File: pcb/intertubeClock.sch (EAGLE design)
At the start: 174 parts, among them Q1 TP5322K1-G, Q10 TP5322K1-G, Q11 TP5322K1-G, Q12 TP5322K1-G, Q13 TP5322K1-G, Q14 TP5322K1-G, Q15 TP5322K1-G, Q16 TP5322K1-G, Q17 NX138AK, Q18 NX138AK, Q19 NX138AK, Q2 TP5322K1-G, Q20 NX138AK, Q21 NX138AK, Q3 TP5322K1-G, Q4 TP5322K1-G, Q5 TP5322K1-G, Q6 TP5322K1-G, Q7 TP5322K1-G, Q8 TP5322K1-G, Q9 TP5322K1-G, U1 HV5122PG, U2 HV5122PG

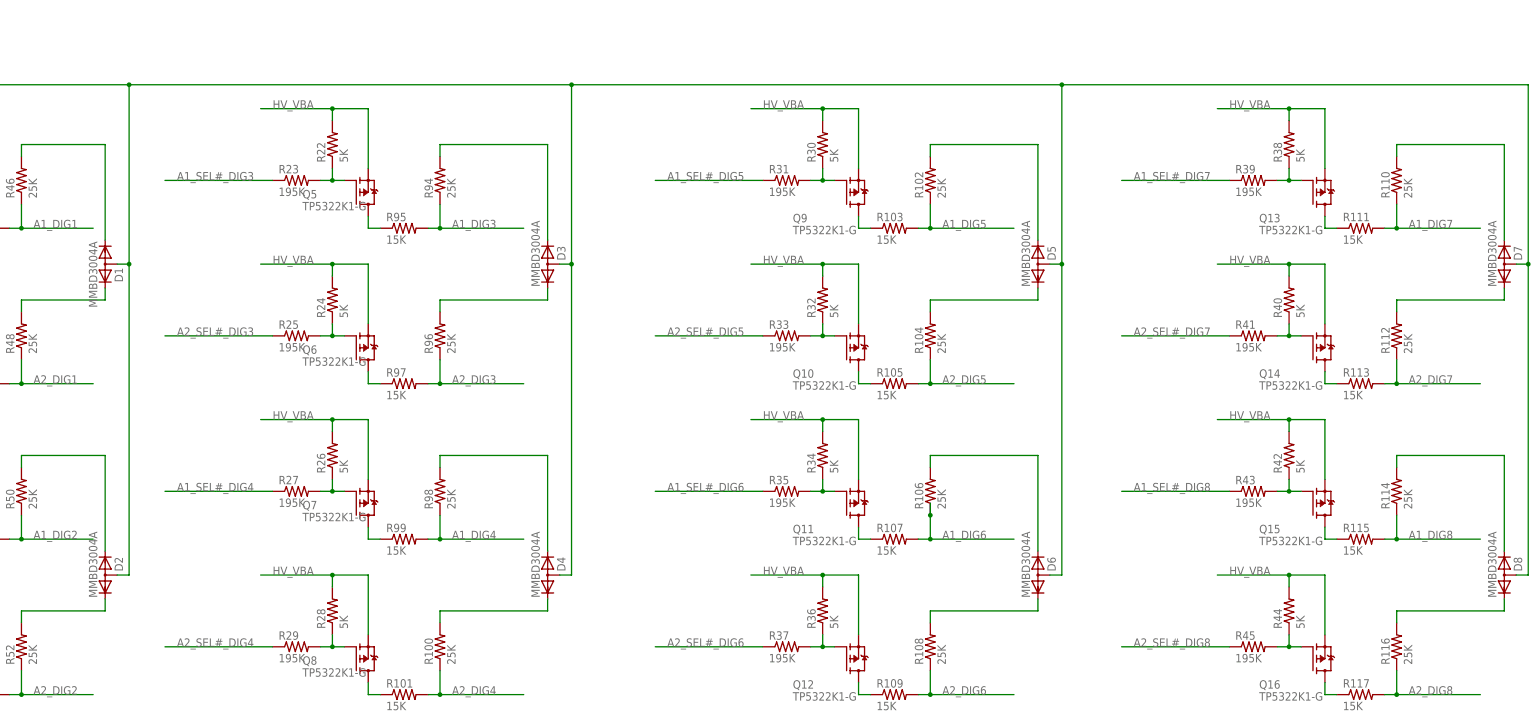
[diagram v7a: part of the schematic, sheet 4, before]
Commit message: -Continued layout. -Pinswapped diodes.
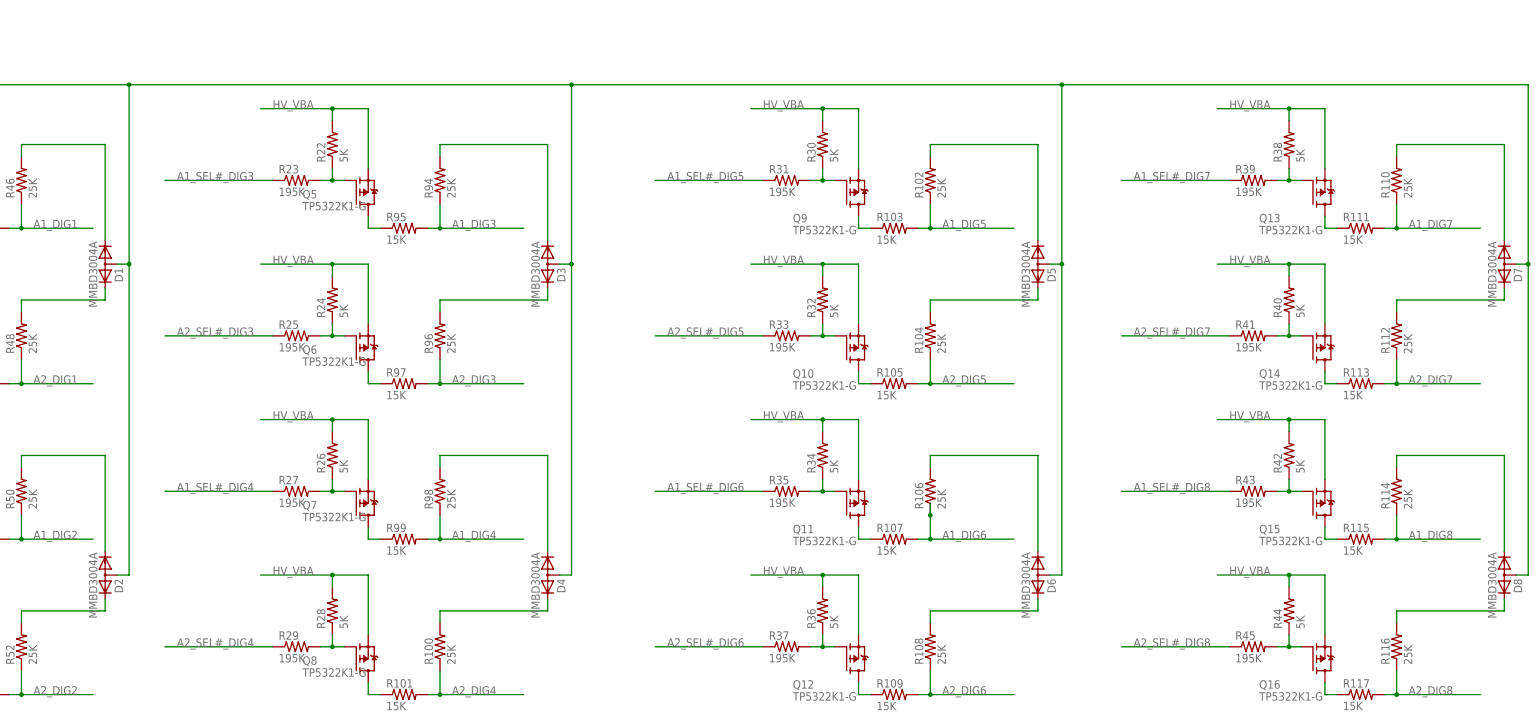
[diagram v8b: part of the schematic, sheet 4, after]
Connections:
- removed net N$40: D3.A
- net HV_VBA_OFF: now also D3.A
- net N$22: now also D2.K1; no longer D2.K2
- net N$25: now also D2.K2; no longer D2.K1
- net N$26: now also D3.K1; no longer D3.K2
- net N$27: now also D3.K2; no longer D3.K1
- net N$28: now also D4.K1; no longer D4.K2
- net N$29: now also D4.K2; no longer D4.K1
- net N$31: now also D5.K1; no longer D5.K2
- net N$32: now also D5.K2; no longer D5.K1
- net N$33: now also D6.K1; no longer D6.K2
- net N$34: now also D6.K2; no longer D6.K1
- net N$36: now also D7.K1; no longer D7.K2
- net N$37: now also D7.K2; no longer D7.K1
- net N$38: now also D8.K1; no longer D8.K2
- net N$39: now also D8.K2; no longer D8.K1
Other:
- note added: "2019.05.10"
- note added: "CONTINUED LAYOUT PINSWAPPED DIODES"
- moved on the sheet: D2, D3, D4, D5, D6, D7, D8
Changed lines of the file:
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@@
 PLACED NEW COMPONENTS
 REPLACED PLACEHOLDERS WITH REAL PARTS</text>
+<text x="50.8" y="162.56" size="2.54" layer="94">ANDERS NELSON</text>
+<text x="144.78" y="162.56" size="2.54" layer="94">2019.05.10</text>
+<text x="193.04" y="165.1" size="2.54" layer="94" rot="MR180">CONTINUED LAYOUT
+PINSWAPPED DIODES</text>
 </plain>
 <instances>
@@
 <instance part="R117" gate="G$1" x="370.84" y="60.96"/>
 <instance part="D1" gate="G$1" x="104.14" y="152.4" rot="R270"/>
-<instance part="D2" gate="G$1" x="104.14" y="86.36" rot="MR90"/>
-<instance part="D3" gate="G$1" x="198.12" y="152.4" rot="MR90"/>
-<instance part="D4" gate="G$1" x="198.12" y="86.36" rot="MR90"/>
-<instance part="D5" gate="G$1" x="302.26" y="152.4" rot="MR90"/>
-<instance part="D6" gate="G$1" x="302.26" y="86.36" rot="MR90"/>
-<instance part="D7" gate="G$1" x="401.32" y="152.4" rot="MR90"/>
-<instance part="D8" gate="G$1" x="401.32" y="86.36" rot="MR90"/>
+<instance part="D2" gate="G$1" x="104.14" y="86.36" rot="R270"/>
+<instance part="D3" gate="G$1" x="198.12" y="152.4" rot="R270"/>
+<instance part="D4" gate="G$1" x="198.12" y="86.36" rot="R270"/>
+<instance part="D5" gate="G$1" x="302.26" y="152.4" rot="R270"/>
+<instance part="D6" gate="G$1" x="302.26" y="86.36" rot="R270"/>
+<instance part="D7" gate="G$1" x="401.32" y="152.4" rot="R270"/>
+<instance part="D8" gate="G$1" x="401.32" y="86.36" rot="R270"/>
 <instance part="Q1" gate="G$1" x="68.58" y="167.64"/>
 <instance part="Q2" gate="G$1" x="68.58" y="134.62"/>
@@
 <pinref part="R50" gate="G$1" pin="2"/>
 <wire x1="86.36" y1="109.22" x2="86.36" y2="111.76" width="0.1524" layer="91"/>
-<wire x1="104.14" y1="91.44" x2="104.14" y2="111.76" width="0.1524" layer="91"/>
 <wire x1="104.14" y1="111.76" x2="86.36" y2="111.76" width="0.1524" layer="91"/>
-<pinref part="D2" gate="G$1" pin="K2"/>
+<pinref part="D2" gate="G$1" pin="K1"/>
+<wire x1="104.14" y1="91.44" x2="104.14" y2="111.76" width="0.1524" layer="91"/>
 </segment>
 </net>
@@
 <wire x1="86.36" y1="76.2" x2="86.36" y2="78.74" width="0.1524" layer="91"/>
 <wire x1="86.36" y1="78.74" x2="104.14" y2="78.74" width="0.1524" layer="91"/>
-<wire x1="104.14" y1="78.74" x2="104.14" y2="81.28" width="0.1524" layer="91"/>
-<pinref part="D2" gate="G$1" pin="K1"/>
+<pinref part="D2" gate="G$1" pin="K2"/>
+<wire x1="104.14" y1="81.28" x2="104.14" y2="78.74" width="0.1524" layer="91"/>
 </segment>
 </net>
@@
 <wire x1="175.26" y1="175.26" x2="175.26" y2="177.8" width="0.1524" layer="91"/>
 <wire x1="175.26" y1="177.8" x2="198.12" y2="177.8" width="0.1524" layer="91"/>
+<pinref part="D3" gate="G$1" pin="K1"/>
 <wire x1="198.12" y1="177.8" x2="198.12" y2="157.48" width="0.1524" layer="91"/>
-<pinref part="D3" gate="G$1" pin="K2"/>
 </segment>
 </net>
@@
 <wire x1="175.26" y1="142.24" x2="175.26" y2="144.78" width="0.1524" layer="91"/>
 <wire x1="175.26" y1="144.78" x2="198.12" y2="144.78" width="0.1524" layer="91"/>
+<pinref part="D3" gate="G$1" pin="K2"/>
 <wire x1="198.12" y1="144.78" x2="198.12" y2="147.32" width="0.1524" layer="91"/>
-<pinref part="D3" gate="G$1" pin="K1"/>
 </segment>
 </net>
@@
 <wire x1="175.26" y1="109.22" x2="175.26" y2="111.76" width="0.1524" layer="91"/>
 <wire x1="175.26" y1="111.76" x2="198.12" y2="111.76" width="0.1524" layer="91"/>
-<wire x1="198.12" y1="111.76" x2="198.12" y2="91.44" width="0.1524" layer="91"/>
-<pinref part="D4" gate="G$1" pin="K2"/>
+<pinref part="D4" gate="G$1" pin="K1"/>
+<wire x1="198.12" y1="91.44" x2="198.12" y2="111.76" width="0.1524" layer="91"/>
 </segment>
 </net>
@@
 <wire x1="175.26" y1="76.2" x2="175.26" y2="78.74" width="0.1524" layer="91"/>
 <wire x1="175.26" y1="78.74" x2="198.12" y2="78.74" width="0.1524" layer="91"/>
-<wire x1="198.12" y1="78.74" x2="198.12" y2="81.28" width="0.1524" layer="91"/>
-<pinref part="D4" gate="G$1" pin="K1"/>
+<pinref part="D4" gate="G$1" pin="K2"/>
+<wire x1="198.12" y1="81.28" x2="198.12" y2="78.74" width="0.1524" layer="91"/>
 </segment>
 </net>
@@
 <wire x1="279.4" y1="175.26" x2="279.4" y2="177.8" width="0.1524" layer="91"/>
 <wire x1="279.4" y1="177.8" x2="302.26" y2="177.8" width="0.1524" layer="91"/>
-<wire x1="302.26" y1="177.8" x2="302.26" y2="157.48" width="0.1524" layer="91"/>
-<pinref part="D5" gate="G$1" pin="K2"/>
+<pinref part="D5" gate="G$1" pin="K1"/>
+<wire x1="302.26" y1="157.48" x2="302.26" y2="177.8" width="0.1524" layer="91"/>
 </segment>
 </net>
@@
 <wire x1="279.4" y1="142.24" x2="279.4" y2="144.78" width="0.1524" layer="91"/>
 <wire x1="279.4" y1="144.78" x2="302.26" y2="144.78" width="0.1524" layer="91"/>
-<wire x1="302.26" y1="144.78" x2="302.26" y2="147.32" width="0.1524" layer="91"/>
-<pinref part="D5" gate="G$1" pin="K1"/>
+<pinref part="D5" gate="G$1" pin="K2"/>
+<wire x1="302.26" y1="147.32" x2="302.26" y2="144.78" width="0.1524" layer="91"/>
 </segment>
 </net>
@@
 <wire x1="279.4" y1="109.22" x2="279.4" y2="111.76" width="0.1524" layer="91"/>
 <wire x1="279.4" y1="111.76" x2="302.26" y2="111.76" width="0.1524" layer="91"/>
+<pinref part="D6" gate="G$1" pin="K1"/>
 <wire x1="302.26" y1="111.76" x2="302.26" y2="91.44" width="0.1524" layer="91"/>
-<pinref part="D6" gate="G$1" pin="K2"/>
 </segment>
 </net>
@@
 <wire x1="279.4" y1="76.2" x2="279.4" y2="78.74" width="0.1524" layer="91"/>
 <wire x1="279.4" y1="78.74" x2="302.26" y2="78.74" width="0.1524" layer="91"/>
+<pinref part="D6" gate="G$1" pin="K2"/>
 <wire x1="302.26" y1="78.74" x2="302.26" y2="81.28" width="0.1524" layer="91"/>
-<pinref part="D6" gate="G$1" pin="K1"/>
 </segment>
 </net>
@@
 <wire x1="378.46" y1="175.26" x2="378.46" y2="177.8" width="0.1524" layer="91"/>
 <wire x1="378.46" y1="177.8" x2="401.32" y2="177.8" width="0.1524" layer="91"/>
+<pinref part="D7" gate="G$1" pin="K1"/>
 <wire x1="401.32" y1="177.8" x2="401.32" y2="157.48" width="0.1524" layer="91"/>
-<pinref part="D7" gate="G$1" pin="K2"/>
 </segment>
 </net>
@@
 <wire x1="378.46" y1="142.24" x2="378.46" y2="144.78" width="0.1524" layer="91"/>
 <wire x1="378.46" y1="144.78" x2="401.32" y2="144.78" width="0.1524" layer="91"/>
+<pinref part="D7" gate="G$1" pin="K2"/>
 <wire x1="401.32" y1="144.78" x2="401.32" y2="147.32" width="0.1524" layer="91"/>
-<pinref part="D7" gate="G$1" pin="K1"/>
 </segment>
 </net>
@@
 <wire x1="378.46" y1="111.76" x2="401.32" y2="111.76" width="0.1524" layer="91"/>
 <wire x1="401.32" y1="111.76" x2="401.32" y2="91.44" width="0.1524" layer="91"/>
-<pinref part="D8" gate="G$1" pin="K2"/>
+<pinref part="D8" gate="G$1" pin="K1"/>
 </segment>
 </net>
@@
 <wire x1="378.46" y1="76.2" x2="378.46" y2="78.74" width="0.1524" layer="91"/>
 <wire x1="378.46" y1="78.74" x2="401.32" y2="78.74" width="0.1524" layer="91"/>
+<pinref part="D8" gate="G$1" pin="K2"/>
 <wire x1="401.32" y1="78.74" x2="401.32" y2="81.28" width="0.1524" layer="91"/>
-<pinref part="D8" gate="G$1" pin="K1"/>
 </segment>
 </net>
@@
 <wire x1="109.22" y1="190.5" x2="109.22" y2="152.4" width="0.1524" layer="91"/>
 <wire x1="109.22" y1="152.4" x2="109.22" y2="86.36" width="0.1524" layer="91"/>
-<wire x1="109.22" y1="86.36" x2="106.68" y2="86.36" width="0.1524" layer="91"/>
 <junction x="203.2" y="190.5"/>
-<wire x1="203.2" y1="190.5" x2="203.2" y2="86.36" width="0.1524" layer="91"/>
-<wire x1="203.2" y1="86.36" x2="200.66" y2="86.36" width="0.1524" layer="91"/>
-<wire x1="304.8" y1="152.4" x2="307.34" y2="152.4" width="0.1524" layer="91"/>
-<wire x1="307.34" y1="152.4" x2="307.34" y2="190.5" width="0.1524" layer="91"/>
+<wire x1="203.2" y1="190.5" x2="203.2" y2="152.4" width="0.1524" layer="91"/>
 <junction x="307.34" y="190.5"/>
+<wire x1="203.2" y1="152.4" x2="203.2" y2="86.36" width="0.1524" layer="91"/>
+<wire x1="307.34" y1="190.5" x2="307.34" y2="152.4" width="0.1524" layer="91"/>
 <wire x1="307.34" y1="152.4" x2="307.34" y2="86.36" width="0.1524" layer="91"/>
-<junction x="307.34" y="152.4"/>
-<wire x1="307.34" y1="86.36" x2="304.8" y2="86.36" width="0.1524" layer="91"/>
-<wire x1="403.86" y1="152.4" x2="406.4" y2="152.4" width="0.1524" layer="91"/>
-<wire x1="406.4" y1="152.4" x2="406.4" y2="190.5" width="0.1524" layer="91"/>
+<wire x1="406.4" y1="190.5" x2="406.4" y2="152.4" width="0.1524" layer="91"/>
+<pinref part="D1" gate="G$1" pin="A"/>
 <wire x1="406.4" y1="152.4" x2="406.4" y2="86.36" width="0.1524" layer="91"/>
-<junction x="406.4" y="152.4"/>
-<wire x1="406.4" y1="86.36" x2="403.86" y2="86.36" width="0.1524" layer="91"/>
-<pinref part="D2" gate="G$1" pin="A"/>
+<wire x1="106.68" y1="152.4" x2="109.22" y2="152.4" width="0.1524" layer="91"/>
+<junction x="109.22" y="152.4"/>
+<pinref part="D3" gate="G$1" pin="A"/>
+<wire x1="200.66" y1="152.4" x2="203.2" y2="152.4" width="0.1524" layer="91"/>
+<junction x="203.2" y="152.4"/>
 <pinref part="D4" gate="G$1" pin="A"/>
+<wire x1="200.66" y1="86.36" x2="203.2" y2="86.36" width="0.1524" layer="91"/>
 <pinref part="D5" gate="G$1" pin="A"/>
+<wire x1="304.8" y1="152.4" x2="307.34" y2="152.4" width="0.1524" layer="91"/>
+<junction x="307.34" y="152.4"/>
 <pinref part="D6" gate="G$1" pin="A"/>
+<wire x1="304.8" y1="86.36" x2="307.34" y2="86.36" width="0.1524" layer="91"/>
 <pinref part="D7" gate="G$1" pin="A"/>
+<wire x1="403.86" y1="152.4" x2="406.4" y2="152.4" width="0.1524" layer="91"/>
+<junction x="406.4" y="152.4"/>
 <pinref part="D8" gate="G$1" pin="A"/>
-<pinref part="D1" gate="G$1" pin="A"/>
-<wire x1="106.68" y1="152.4" x2="109.22" y2="152.4" width="0.1524" layer="91"/>
-<junction x="109.22" y="152.4"/>
-</segment>
-</net>
-<net name="N$40" class="0">
-<segment>
-<junction x="203.2" y="152.4"/>
-<wire x1="200.66" y1="152.4" x2="203.2" y2="152.4" width="0.1524" layer="91"/>
-<pinref part="D3" gate="G$1" pin="A"/>
+<wire x1="406.4" y1="86.36" x2="403.86" y2="86.36" width="0.1524" layer="91"/>
+<pinref part="D2" gate="G$1" pin="A"/>
+<wire x1="109.22" y1="86.36" x2="106.68" y2="86.36" width="0.1524" layer="91"/>
 </segment>
 </net>
